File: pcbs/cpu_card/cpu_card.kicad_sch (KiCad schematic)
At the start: 12 parts, among them J1 Conn1, J2 osc_header, U1 74LS161, Y1 ECS-2100AX-100

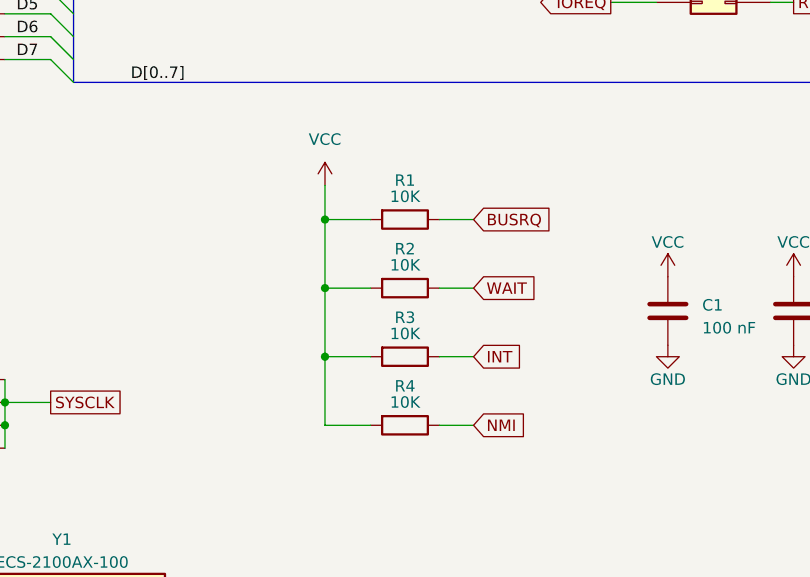
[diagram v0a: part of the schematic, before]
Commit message: Changed Z80 input pull-up resistors to lower values to account for transition time at 10Mhz
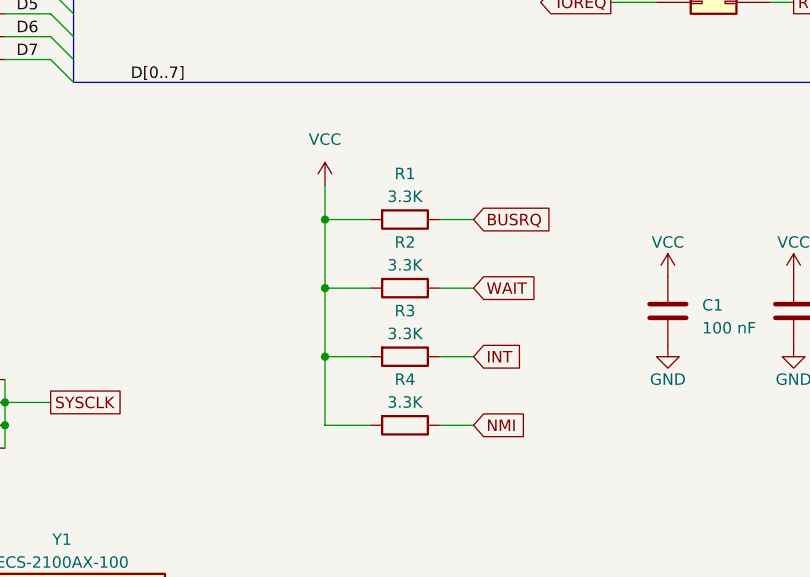
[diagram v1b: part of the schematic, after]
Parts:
- R1, R2, R3, R4: value 10K -> 3.3K
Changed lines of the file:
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@@
     (in_bom yes) (on_board yes) (dnp no) (fields_autoplaced)
     (property "Reference" "R2" (at 166.37 139.7 90)
-      (effects (font (size 1.27 1.27)) (justify top))
-    )
-    (property "Value" "10K" (at 166.37 142.24 90)
+      (effects (font (size 1.27 1.27)))
+    )
+    (property "Value" "3.3K" (at 166.37 142.24 90)
       (effects (font (size 1.27 1.27)))
     )
@@
     (in_bom yes) (on_board yes) (dnp no) (fields_autoplaced)
     (property "Reference" "R4" (at 166.37 154.94 90)
-      (effects (font (size 1.27 1.27)) (justify top))
-    )
-    (property "Value" "10K" (at 166.37 157.48 90)
+      (effects (font (size 1.27 1.27)))
+    )
+    (property "Value" "3.3K" (at 166.37 157.48 90)
       (effects (font (size 1.27 1.27)))
     )
@@
     (in_bom yes) (on_board yes) (dnp no) (fields_autoplaced)
     (property "Reference" "R1" (at 166.37 132.08 90)
-      (effects (font (size 1.27 1.27)) (justify top))
-    )
-    (property "Value" "10K" (at 166.37 134.62 90)
+      (effects (font (size 1.27 1.27)))
+    )
+    (property "Value" "3.3K" (at 166.37 134.62 90)
       (effects (font (size 1.27 1.27)))
     )
@@
     (in_bom yes) (on_board yes) (dnp no) (fields_autoplaced)
     (property "Reference" "R3" (at 166.37 147.32 90)
-      (effects (font (size 1.27 1.27)) (justify top))
-    )
-    (property "Value" "10K" (at 166.37 149.86 90)
-      (effects (font (size 1.27 1.27)))
-    )
+      (effects (font (size 1.27 1.27)))
+    )
+    (property "Value" "3.3K" (at 166.37 149.86 90)
+      (effects (font (size 1.27 1.27)))
+    )

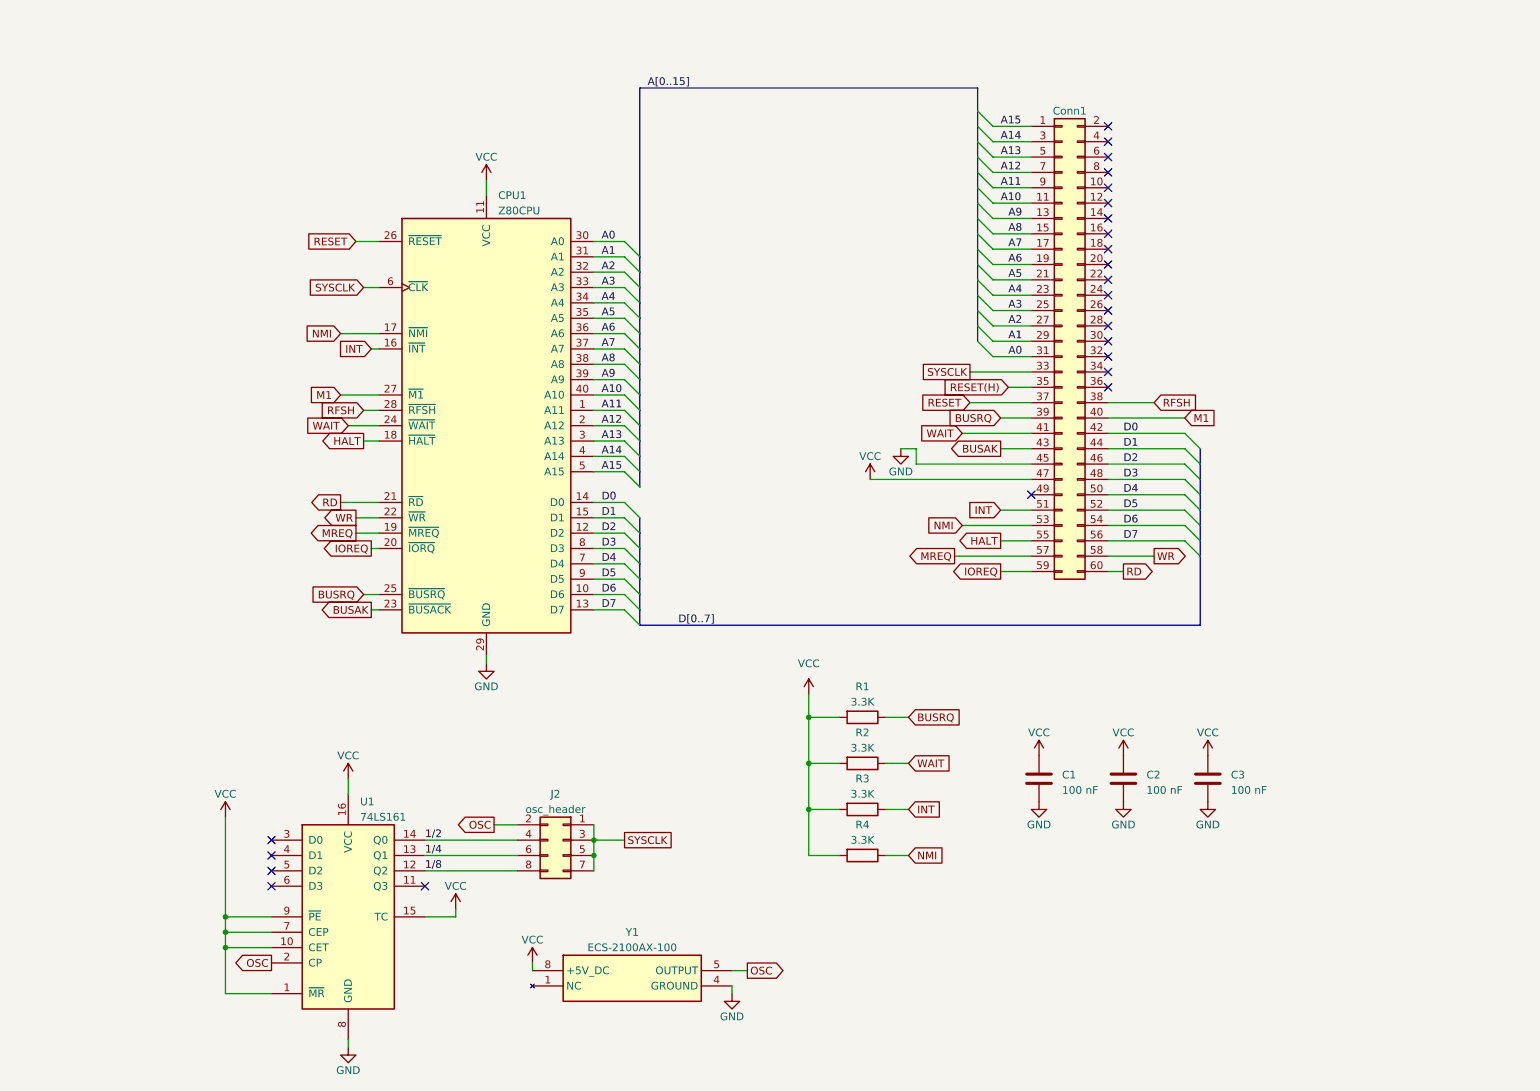
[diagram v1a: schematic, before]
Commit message: Changed the bus hardware to 2.54mm header and cleaned up the CPU card PCB layout
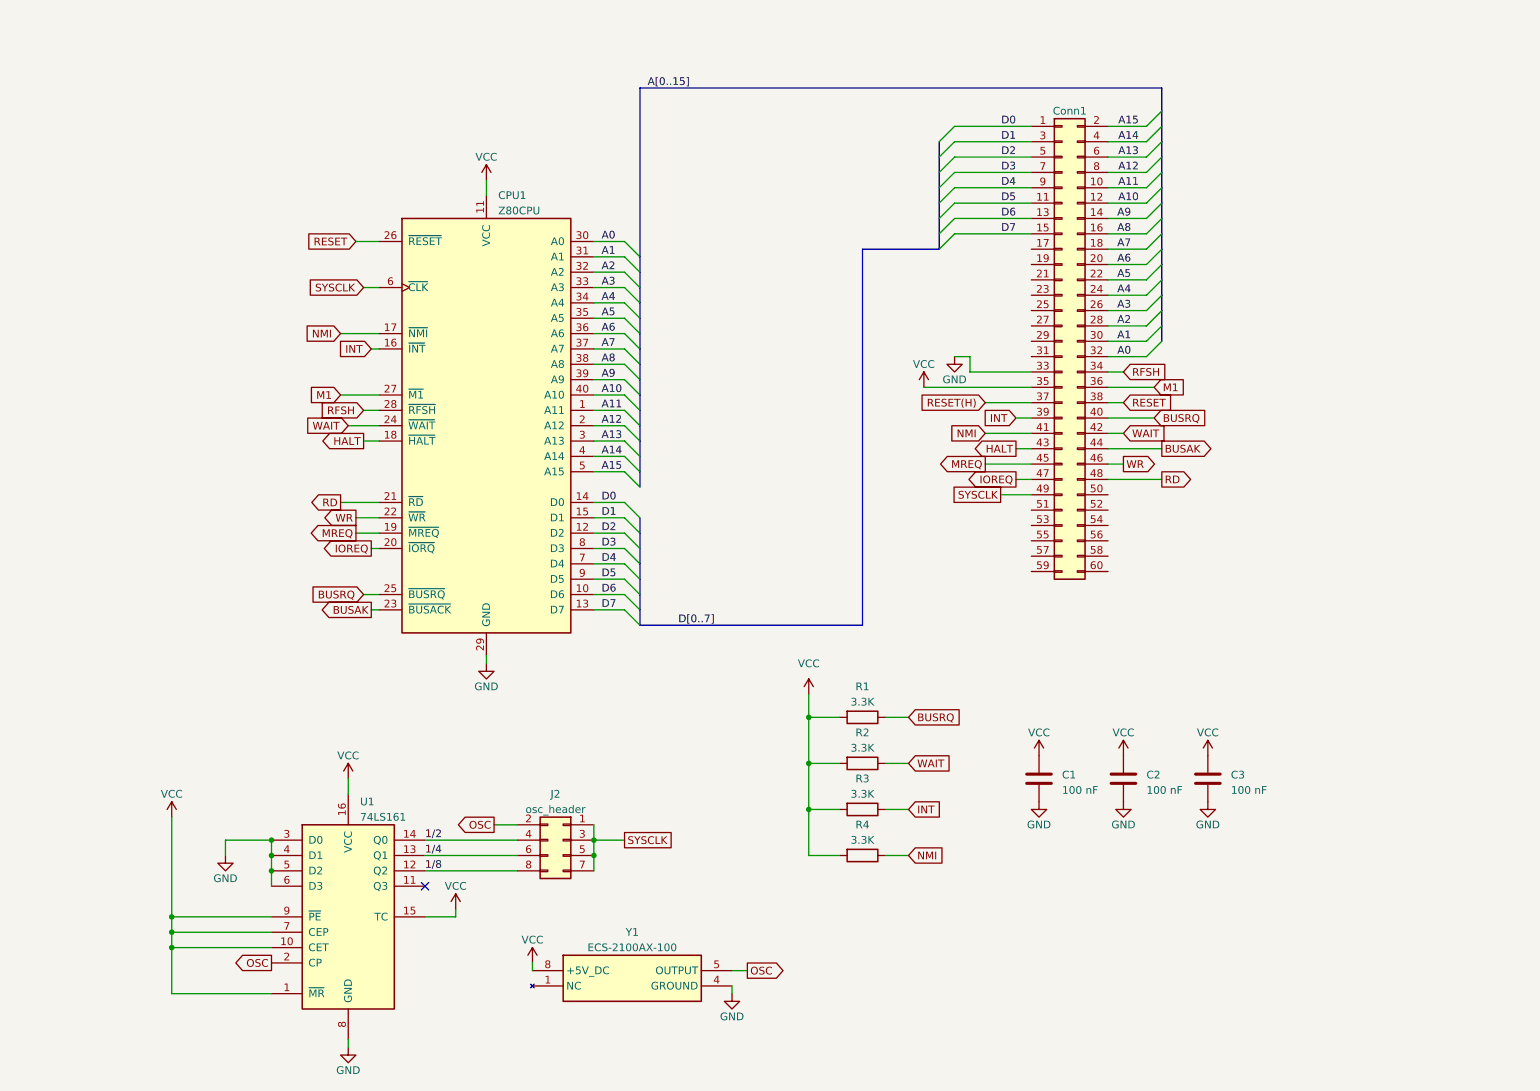
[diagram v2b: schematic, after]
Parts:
- J1: footprint Z80 Parts:2x30-edge-connector -> Connector_PinHeader_2.54mm:PinHeader_2x30_P2.54mm_Vertical
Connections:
- net A0: now also J1.32 (Pin_32); no longer J1.31 (Pin_31)
- net A1: now also J1.30 (Pin_30); no longer J1.29 (Pin_29)
- net A10: now also J1.12 (Pin_12); no longer J1.11 (Pin_11)
- net A11: now also J1.10 (Pin_10); no longer J1.9 (Pin_9)
- net A12: now also J1.8 (Pin_8); no longer J1.7 (Pin_7)
- net A13: now also J1.6 (Pin_6); no longer J1.5 (Pin_5)
- net A14: now also J1.4 (Pin_4); no longer J1.3 (Pin_3)
- net A15: now also J1.2 (Pin_2); no longer J1.1 (Pin_1)
- net A2: now also J1.28 (Pin_28); no longer J1.27 (Pin_27)
- net A3: now also J1.26 (Pin_26); no longer J1.25 (Pin_25)
- net A4: now also J1.24 (Pin_24); no longer J1.23 (Pin_23)
- net A5: now also J1.22 (Pin_22); no longer J1.21 (Pin_21)
- net A6: now also J1.20 (Pin_20); no longer J1.19 (Pin_19)
- net A7: now also J1.18 (Pin_18); no longer J1.17 (Pin_17)
- net A8: now also J1.16 (Pin_16); no longer J1.15 (Pin_15)
- net A9: now also J1.14 (Pin_14); no longer J1.13 (Pin_13)
- net BUSAK: now also J1.44 (Pin_44); no longer J1.43 (Pin_43)
- net BUSRQ: now also J1.40 (Pin_40); no longer J1.39 (Pin_39)
- net D0: now also J1.1 (Pin_1); no longer J1.42 (Pin_42)
- net D1: now also J1.3 (Pin_3); no longer J1.44 (Pin_44)
- net D2: now also J1.5 (Pin_5); no longer J1.46 (Pin_46)
- net D3: now also J1.7 (Pin_7); no longer J1.48 (Pin_48)
- net D4: now also J1.9 (Pin_9); no longer J1.50 (Pin_50)
- net D5: now also J1.11 (Pin_11); no longer J1.52 (Pin_52)
- net D6: now also J1.13 (Pin_13); no longer J1.54 (Pin_54)
- net D7: now also J1.15 (Pin_15); no longer J1.56 (Pin_56)
- net GND: now also J1.33 (Pin_33), U1.3 (D0), U1.4 (D1), U1.5 (D2), U1.6 (D3); no longer J1.45 (Pin_45)
- net HALT: now also J1.43 (Pin_43); no longer J1.55 (Pin_55)
- net INT: now also J1.39 (Pin_39); no longer J1.51 (Pin_51)
- net IOREQ: now also J1.47 (Pin_47); no longer J1.59 (Pin_59)
- net M1: now also J1.36 (Pin_36); no longer J1.40 (Pin_40)
- net MREQ: now also J1.45 (Pin_45); no longer J1.57 (Pin_57)
- net NMI: now also J1.41 (Pin_41); no longer J1.53 (Pin_53)
- net RD: now also J1.48 (Pin_48); no longer J1.60 (Pin_60)
- net RESET: now also J1.38 (Pin_38); no longer J1.37 (Pin_37)
- net RESET(H): now also J1.37 (Pin_37); no longer J1.35 (Pin_35)
- net RFSH: now also J1.34 (Pin_34); no longer J1.38 (Pin_38)
- net SYSCLK: now also J1.49 (Pin_49); no longer J1.33 (Pin_33)
- net VCC: now also J1.35 (Pin_35); no longer J1.47 (Pin_47)
- net WAIT: now also J1.42 (Pin_42); no longer J1.41 (Pin_41)
- net WR: now also J1.46 (Pin_46); no longer J1.58 (Pin_58)
- no-connect marks 24 -> 1

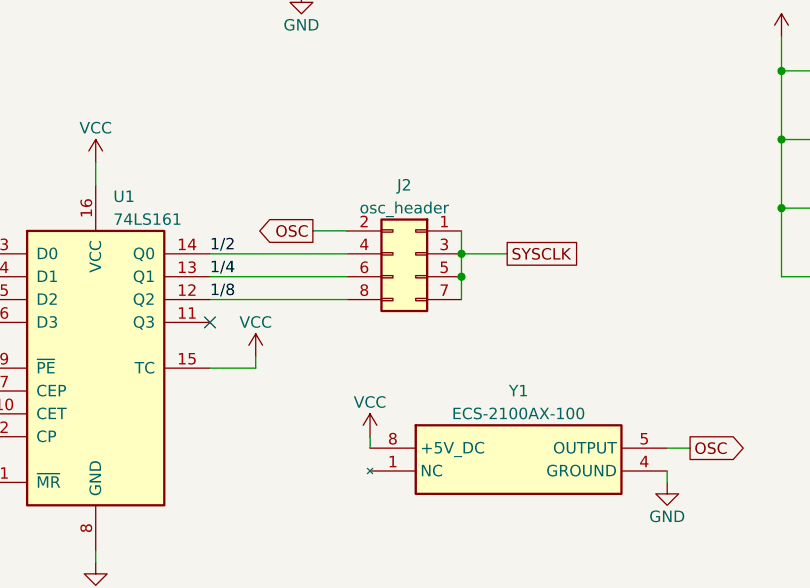
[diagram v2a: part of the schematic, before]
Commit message: Changed CPU board to nominal 20MHz with the option to adjust using the 2x5 header.
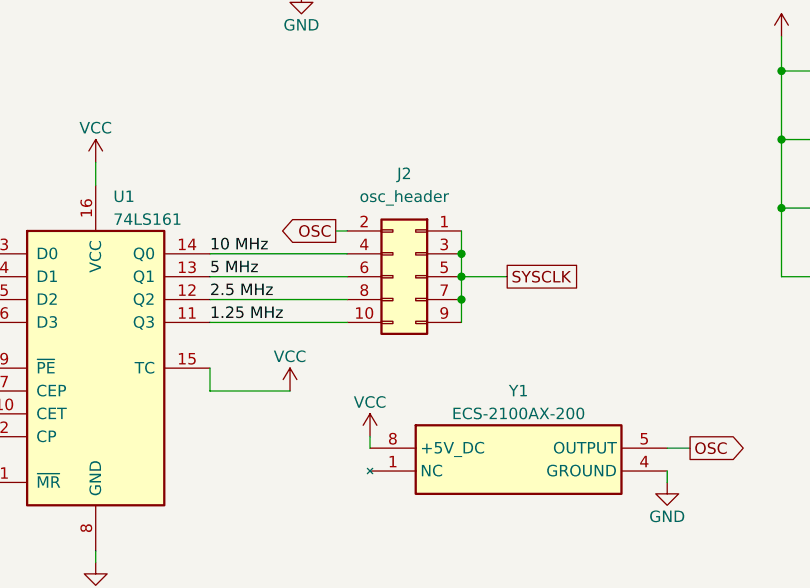
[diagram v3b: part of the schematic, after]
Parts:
- removed J2: osc_header, Connector_PinHeader_2.54mm:PinHeader_2x04_P2.54mm_Vertical, symbol Connector_Generic:Conn_02x04_Odd_Even
- added J2: osc_header, Connector_PinHeader_2.54mm:PinHeader_2x05_P2.54mm_Vertical, symbol Connector_Generic:Conn_02x05_Odd_Even
- Y1: value ECS-2100AX-100 -> ECS-2100AX-200; footprint Z80 Parts:ECS-2100AX-100 -> Z80 Parts:ECS-2100AX-200; symbol Z80 Parts:ECS-2100AX-100 -> Z80 Parts:ECS-2100AX-200
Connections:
- net OSC: now also J2.2 (Pin_2)
- net SYSCLK: now also J2.1 (Pin_1), J2.3 (Pin_3), J2.5 (Pin_5), J2.7 (Pin_7), J2.9 (Pin_9)
- net 1.25 MHz: now reaches U1.11 (Q3)
- net 1.25 MHz: now also J2.10 (Pin_10)
- net 1/2 renamed 10 MHz
- net 10 MHz: now also J2.4 (Pin_4)
- net 1/4 renamed 5 MHz
- net 5 MHz: now also J2.6 (Pin_6)
- net 1/8 renamed 2.5 MHz
- net 2.5 MHz: now also J2.8 (Pin_8)
- no-connect marks 1 -> 0
